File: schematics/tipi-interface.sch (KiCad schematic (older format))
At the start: 29 parts

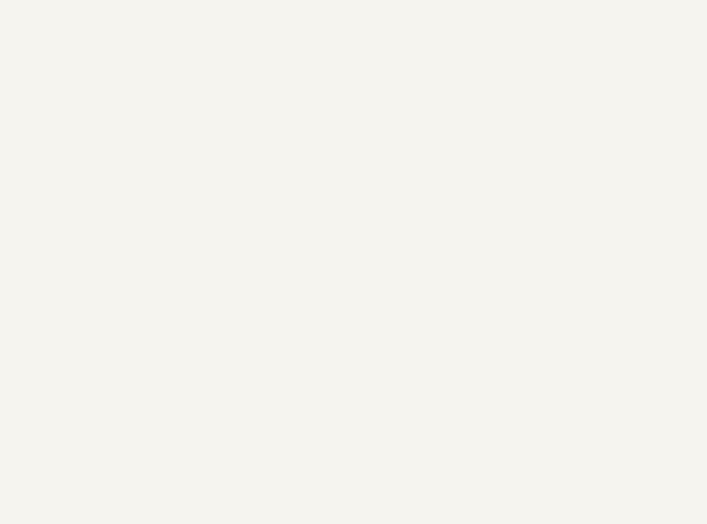
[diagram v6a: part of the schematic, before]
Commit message: new schematic targing Xilinx CPLD
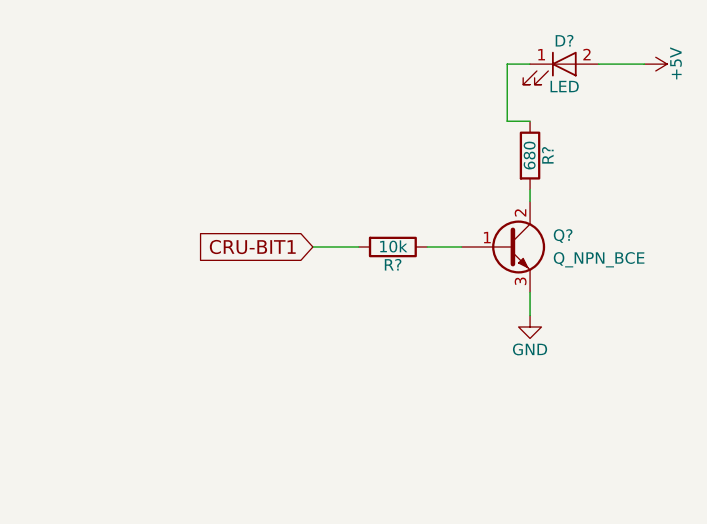
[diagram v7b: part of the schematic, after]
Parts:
- added D?: LED, symbol LED
- added Q?: Q_NPN_BCE, symbol Q_NPN_BCE
- added R?: 680, symbol R
- added R?: 10k, symbol R
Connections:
- net +5V: now also D?.2 (A)
- net CRU-BIT1: now also R?.2
- net GND: now also Q?.3 (E)
- new net: D?.1 (K), R?.1
- new net: Q?.1 (B), R?.1
- new net: Q?.2 (C), R?.2
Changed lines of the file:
@@
 Text GLabel 10000 7300 2    60   Input ~ 0
 BCM-21
+$Comp
+L LED D?
+U 1 1 588E625B
+P 13900 800
+F 0 "D?" H 13900 900 50  0000 C CNN
+F 1 "LED" H 13900 700 50  0000 C CNN
+F 2 "" H 13900 800 50  0000 C CNN
+F 3 "" H 13900 800 50  0000 C CNN
+	1    13900 800
+	1    0    0    -1
+$EndComp
+$Comp
+L Q_NPN_BCE Q?
+U 1 1 588E6302
+P 13650 1600
+F 0 "Q?" H 13850 1650 50  0000 L CNN
+F 1 "Q_NPN_BCE" H 13850 1550 50  0000 L CNN
+F 2 "" H 13850 1700 50  0000 C CNN
+F 3 "" H 13650 1600 50  0000 C CNN
+	1    13650 1600
+	1    0    0    -1
+$EndComp
+$Comp
+L +5V #PWR?
+U 1 1 588E642B
+P 14250 800
+F 0 "#PWR?" H 14250 650 50  0001 C CNN
+F 1 "+5V" H 14250 940 50  0000 C CNN
+F 2 "" H 14250 800 50  0000 C CNN
+F 3 "" H 14250 800 50  0000 C CNN
+	1    14250 800
+	0    1    1    0
+$EndComp
+$Comp
+L GND #PWR?
+U 1 1 588E649C
+P 13750 1900
+F 0 "#PWR?" H 13750 1650 50  0001 C CNN
+F 1 "GND" H 13750 1750 50  0000 C CNN
+F 2 "" H 13750 1900 50  0000 C CNN
+F 3 "" H 13750 1900 50  0000 C CNN
+	1    13750 1900
+	1    0    0    -1
+$EndComp
+Text GLabel 12800 1600 0    60   Input ~ 0
+CRU-BIT1
+$Comp
+L R R?
+U 1 1 588E654C
+P 13750 1200
+F 0 "R?" V 13830 1200 50  0000 C CNN
+F 1 "680" V 13750 1200 50  0000 C CNN
+F 2 "" V 13680 1200 50  0000 C CNN
+F 3 "" H 13750 1200 50  0000 C CNN
+	1    13750 1200
+	1    0    0    -1
+$EndComp
+$Comp
+L R R?
+U 1 1 588E6609
+P 13150 1600
+F 0 "R?" V 13230 1600 50  0000 C CNN
+F 1 "10k" V 13150 1600 50  0000 C CNN
+F 2 "" V 13080 1600 50  0000 C CNN
+F 3 "" H 13150 1600 50  0000 C CNN
+	1    13150 1600
+	0    1    1    0
+$EndComp
+Wire Wire Line
+	12800 1600 13000 1600
+Wire Wire Line
+	13300 1600 13450 1600
+Wire Wire Line
+	13750 1800 13750 1900
+Wire Wire Line
+	13750 1400 13750 1350
+Wire Wire Line
+	13750 1050 13650 1050
+Wire Wire Line
+	13650 1050 13650 800
+Wire Wire Line
+	13650 800  13750 800
+Wire Wire Line
+	14050 800  14250 800
 $EndSCHEMATC
